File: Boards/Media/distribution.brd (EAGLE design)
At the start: 37.8 x 58.4 mm, 16 parts

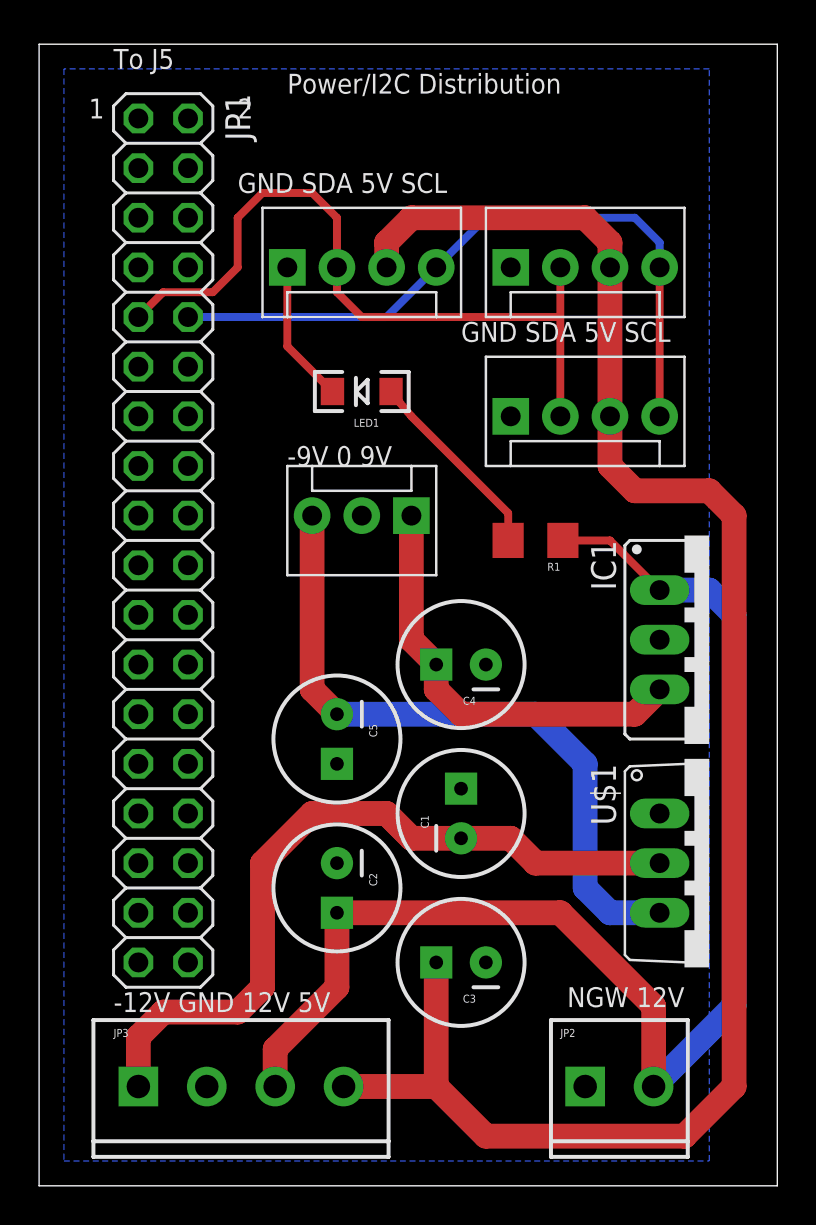
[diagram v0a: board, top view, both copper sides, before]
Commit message: Changed to a PI GPIO header (ditching the NGW100)
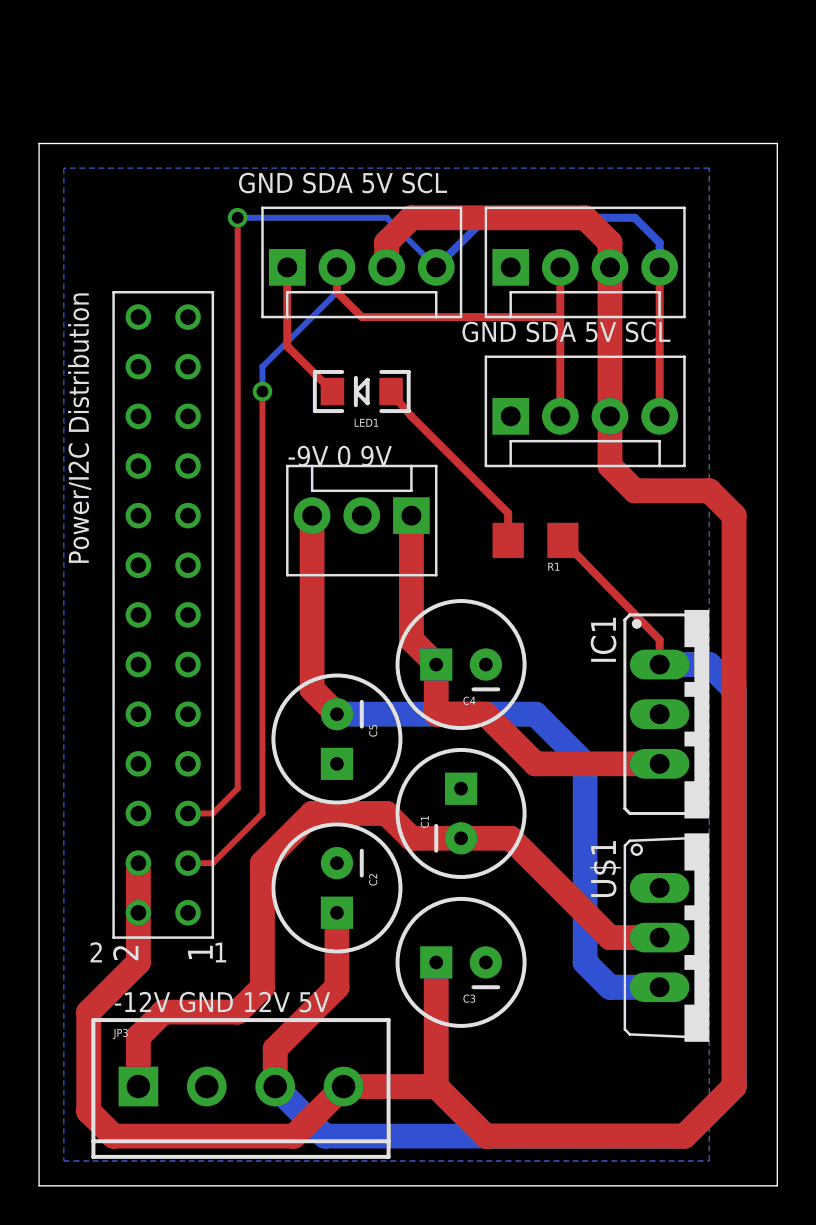
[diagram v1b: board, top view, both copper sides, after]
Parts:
- removed JP1: (no value), pinhead:2X18
- removed JP2: 12V Out NGW, 1_SparkFun-Connectors:SCREWTERMINAL-3.5MM-2
- added U$2: PI-GPIO, 0_Tristan's_Lib:M2X13
- moved IC1 3.81 mm to (34.3, 24.1)
- moved U$1 3.81 mm to (31.8, 12.7)
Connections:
- net 12V: no longer JP2.2
- net 5V: now also U$2.2, U$2.4
- net GND: now also U$2.14, U$2.20, U$2.25, U$2.6, U$2.9; no longer JP1.2, JP1.34, JP1.36, JP2.1
- net SCL: now also U$2.5; no longer JP1.10
- net SDA: now also U$2.3; no longer JP1.9
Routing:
- net SCL: track 35.7 -> 65.4 mm, vias 0 -> 1
- net 5V: track 90.2 -> 118.6 mm
- net SDA: track 38.2 -> 55.2 mm, vias 0 -> 1
- net -9V: track 35.1 -> 38.9 mm
- net -12V: track 38.7 -> 40.3 mm
- net 9V: track 21.9 -> 23.2 mm
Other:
- board size 37.8 x 58.4 mm -> 37.8 x 53.3 mm
- board text removed: "NGW 12V"
- board text removed: "To J5"

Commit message: DSP sch nearly complete, added most components. Still needs reset generator and final check
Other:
- board text added: "T. Honscheid 11/2014"
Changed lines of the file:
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@@
 <text x="12.7" y="36.83" size="1.016" layer="21">-9V 0 9V</text>
 <text x="3.81" y="8.89" size="1.016" layer="21">-12V GND 12V 5V</text>
+<text x="19.05" y="1.27" size="1.016" layer="21">T. Honscheid 11/2014</text>
 </plain>
 <attributes>

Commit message: Prepared board for production, last minute error checks and rotations
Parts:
- added JP1: UART, 1_SparkFun-Connectors:MOLEX-1X3
- added R2, R3, R4, R5: 2k2, 1_SparkFun-Resistors:1206
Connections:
- new net N$2: R2.2, R3.2, U$2.1
- new net N$3: R4.2, U$2.8
- new net N$4: R5.1, U$2.10
- new net N$5: JP1.1, R4.1
- new net N$6: JP1.3, R5.2
- net GND: now also JP1.2
- net SCL: now also R3.1
- net SDA: now also R2.1
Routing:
- net N$5: track 0.00 -> 28.8 mm
- net N$6: track 0.00 -> 24.2 mm
- net SDA: track 55.2 -> 66.0 mm
- net N$2: track 0.00 -> 6.22 mm
- net SCL: track 65.4 -> 69.3 mm
- net N$3: track 0.00 -> 3.78 mm
- net N$4: track 0.00 -> 3.58 mm
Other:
- board size 37.8 x 53.3 mm -> 37.8 x 55.9 mm
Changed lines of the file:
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@@
 <setting verticaltext="up"/>
 </settings>
-<grid distance="0.05" unitdist="inch" unit="inch" style="lines" multiple="1" display="no" altdistance="0.025" altunitdist="inch" altunit="inch"/>
+<grid distance="0.01" unitdist="inch" unit="inch" style="lines" multiple="1" display="no" altdistance="0.025" altunitdist="inch" altunit="inch"/>
 <layers>
 <layer number="1" name="Top" color="4" fill="1" visible="yes" active="yes"/>
@@
 <plain>
 <wire x1="0" y1="0" x2="37.77" y2="0" width="0" layer="20"/>
-<wire x1="37.77" y1="0" x2="37.77" y2="53.33" width="0" layer="20"/>
-<wire x1="37.77" y1="53.33" x2="0" y2="53.33" width="0" layer="20"/>
-<wire x1="0" y1="53.33" x2="0" y2="0" width="0" layer="20"/>
-<text x="2.54" y="31.75" size="1.016" layer="21" rot="R90">Power/I2C Distribution</text>
+<wire x1="37.77" y1="0" x2="37.77" y2="55.87" width="0" layer="20"/>
+<wire x1="37.77" y1="55.87" x2="0" y2="55.87" width="0" layer="20"/>
+<wire x1="0" y1="55.87" x2="0" y2="0" width="0" layer="20"/>
+<text x="36.576" y="36.068" size="1.016" layer="21" rot="R90">Power/I2C Distribution</text>
 <text x="8.89" y="11.43" size="1.016" layer="21">1</text>
 <text x="2.54" y="11.43" size="1.016" layer="21">2</text>
-<text x="10.16" y="50.8" size="1.016" layer="21">GND SDA 5V SCL</text>
+<text x="11.43" y="50.8" size="1.016" layer="21">GND SDA 5V SCL</text>
 <text x="21.59" y="43.18" size="1.016" layer="21">GND SDA 5V SCL</text>
 <text x="12.7" y="36.83" size="1.016" layer="21">-9V 0 9V</text>
@@
 <element name="U$1" library="0_Tristan's_Lib" package="TO-220V" value="VREG-GIO" x="31.75" y="12.7" rot="R270"/>
 <element name="U$2" library="0_Tristan's_Lib" package="M2X13" value="PI-GPIO" x="6.35" y="13.97" rot="R90"/>
+<element name="JP1" library="1_SparkFun-Connectors" package="MOLEX-1X3" value="UART" x="2.54" y="50.8"/>
+<element name="R2" library="1_SparkFun-Resistors" package="1206" value="2k2" x="11.43" y="12.7" rot="MR90"/>
+<element name="R3" library="1_SparkFun-Resistors" package="1206" value="2k2" x="11.43" y="17.78" rot="MR270"/>
+<element name="R4" library="1_SparkFun-Resistors" package="1206" value="2k2" x="1.778" y="21.844" rot="R270"/>
+<element name="R5" library="1_SparkFun-Resistors" package="1206" value="2k2" x="2.286" y="27.432" rot="R90"/>
 </elements>
 <signals>
@@
 <vertex x="1.27" y="1.27"/>
 <vertex x="34.29" y="1.27"/>
-<vertex x="34.29" y="52.07"/>
-<vertex x="1.27" y="52.07"/>
+<vertex x="34.29" y="54.61"/>
+<vertex x="1.27" y="54.61"/>
 </polygon>
 <wire x1="12.7" y1="46.99" x2="12.7" y2="42.95" width="0.4064" layer="1"/>
@@
 <contactref element="U$2" pad="14"/>
 <contactref element="U$2" pad="9"/>
+<contactref element="JP1" pad="2"/>
 </signal>
 <signal name="SCL">
@@
 <wire x1="10.16" y1="49.53" x2="17.78" y2="49.53" width="0.3048" layer="16"/>
 <wire x1="17.78" y1="49.53" x2="20.32" y2="46.99" width="0.3048" layer="16"/>
+<contactref element="R3" pad="1"/>
+<wire x1="11.43" y1="19.18" x2="7.62" y2="19.18" width="0.4064" layer="16"/>
+<wire x1="7.62" y1="19.18" x2="7.62" y2="19.05" width="0.4064" layer="16"/>
 </signal>
 <signal name="SDA">
@@
 <wire x1="11.43" y1="41.91" x2="15.24" y2="45.72" width="0.3048" layer="16"/>
 <wire x1="15.24" y1="45.72" x2="15.24" y2="46.99" width="0.3048" layer="16"/>
+<contactref element="R2" pad="1"/>
+<wire x1="11.43" y1="11.3" x2="6.48" y2="11.3" width="0.4064" layer="16"/>
+<wire x1="6.48" y1="11.3" x2="6.35" y2="11.43" width="0.4064" layer="16"/>
+<wire x1="6.35" y1="11.43" x2="6.35" y2="15.24" width="0.4064" layer="16"/>
+<wire x1="6.35" y1="15.24" x2="7.62" y2="16.51" width="0.4064" layer="16"/>
 </signal>
 <signal name="12V">
@@
 <wire x1="29.21" y1="10.16" x2="31.75" y2="10.16" width="1.27" layer="16"/>
 </signal>
+<signal name="N$2">
+<contactref element="U$2" pad="1"/>
+<contactref element="R2" pad="2"/>
+<contactref element="R3" pad="2"/>
+<wire x1="11.43" y1="16.38" x2="11.43" y2="14.1" width="0.4064" layer="16"/>
+<wire x1="11.43" y1="14.1" x2="7.62" y2="14.1" width="0.4064" layer="16"/>
+<wire x1="7.62" y1="14.1" x2="7.62" y2="13.97" width="0.4064" layer="16"/>
+</signal>
+<signal name="N$3">
+<contactref element="U$2" pad="8"/>
+<contactref element="R4" pad="2"/>
+<wire x1="5.08" y1="21.59" x2="4.318" y2="21.59" width="0.3048" layer="1"/>
+<wire x1="4.318" y1="21.59" x2="3.302" y2="20.574" width="0.3048" layer="1"/>
+<wire x1="3.302" y1="20.574" x2="1.908" y2="20.574" width="0.3048" layer="1"/>
+<wire x1="1.908" y1="20.574" x2="1.778" y2="20.444" width="0.3048" layer="1"/>
+</signal>
+<signal name="N$4">
+<contactref element="U$2" pad="10"/>
+<contactref element="R5" pad="1"/>
+<wire x1="5.08" y1="24.13" x2="4.188" y2="24.13" width="0.3048" layer="1"/>
+<wire x1="4.188" y1="24.13" x2="2.286" y2="26.032" width="0.3048" layer="1"/>
+</signal>
+<signal name="N$5">
+<contactref element="R4" pad="1"/>
+<contactref element="JP1" pad="1"/>
+<wire x1="1.778" y1="23.244" x2="1.648" y2="23.244" width="0.3048" layer="1"/>
+<wire x1="1.648" y1="23.244" x2="0.762" y2="24.13" width="0.3048" layer="1"/>
+<wire x1="0.762" y1="24.13" x2="0.762" y2="30.734" width="0.3048" layer="1"/>
+<wire x1="0.762" y1="30.734" x2="2.032" y2="32.004" width="0.3048" layer="1"/>
+<wire x1="2.032" y1="32.004" x2="2.032" y2="50.292" width="0.3048" layer="1"/>
+<wire x1="2.032" y1="50.292" x2="2.54" y2="50.8" width="0.3048" layer="1"/>
+</signal>
+<signal name="N$6">
+<contactref element="JP1" pad="3"/>
+<contactref element="R5" pad="2"/>
+<wire x1="2.286" y1="28.832" x2="2.286" y2="31.242" width="0.3048" layer="1"/>
+<wire x1="2.286" y1="31.242" x2="2.794" y2="31.75" width="0.3048" layer="1"/>
+<wire x1="2.794" y1="31.75" x2="2.794" y2="45.974" width="0.3048" layer="1"/>
+<wire x1="2.794" y1="45.974" x2="7.62" y2="50.8" width="0.3048" layer="1"/>
+</signal>
 </signals>
